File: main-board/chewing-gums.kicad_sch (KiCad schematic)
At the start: 14 parts

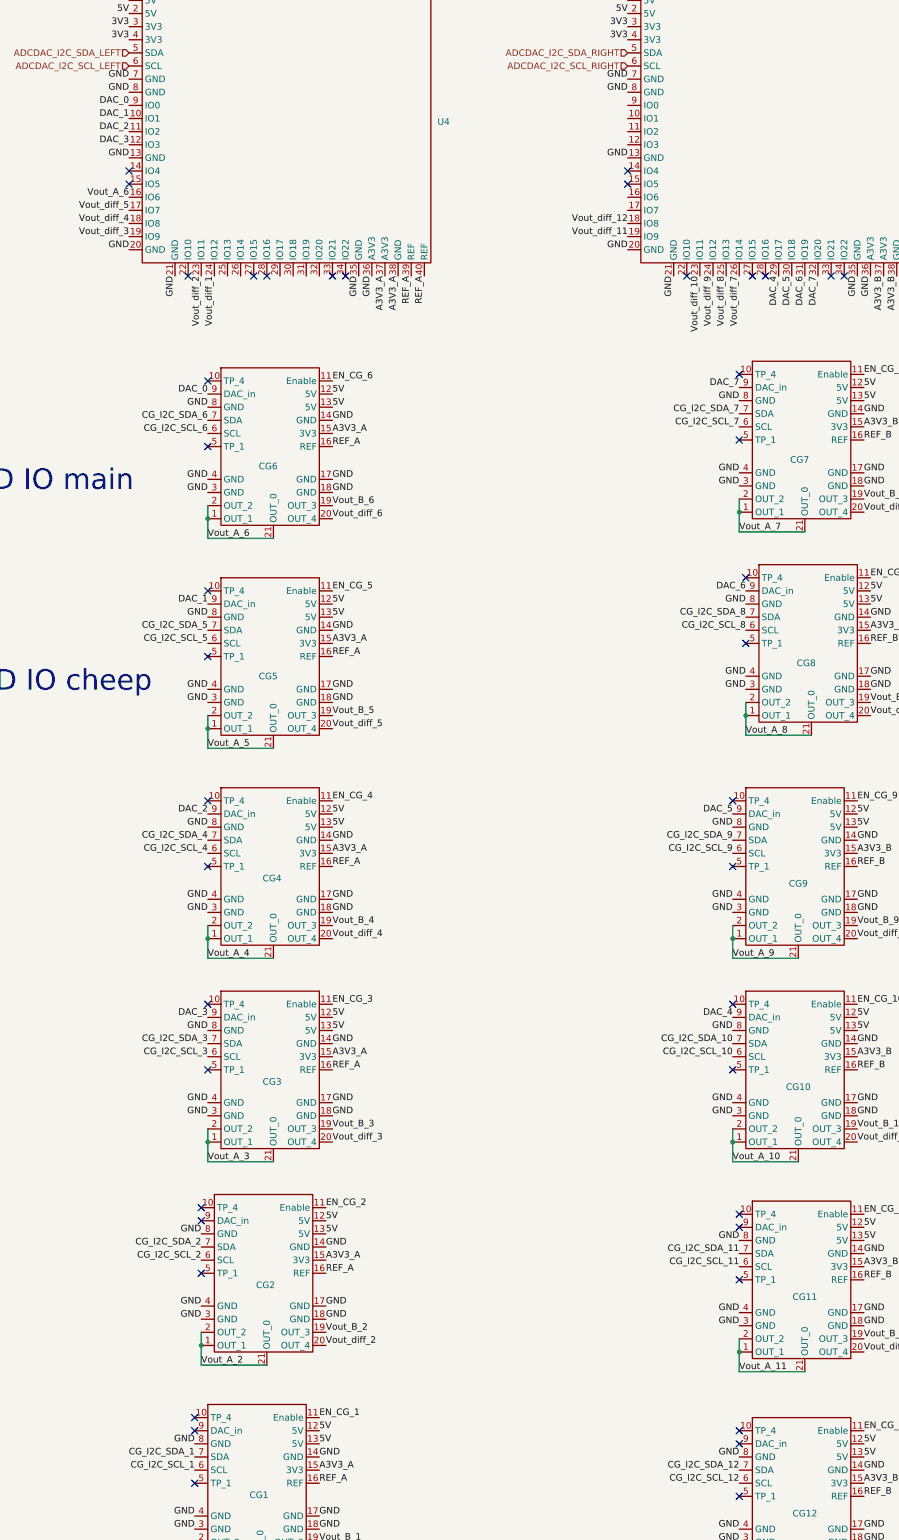
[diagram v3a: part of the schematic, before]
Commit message: Routed all power signals and re-organized GPIOs
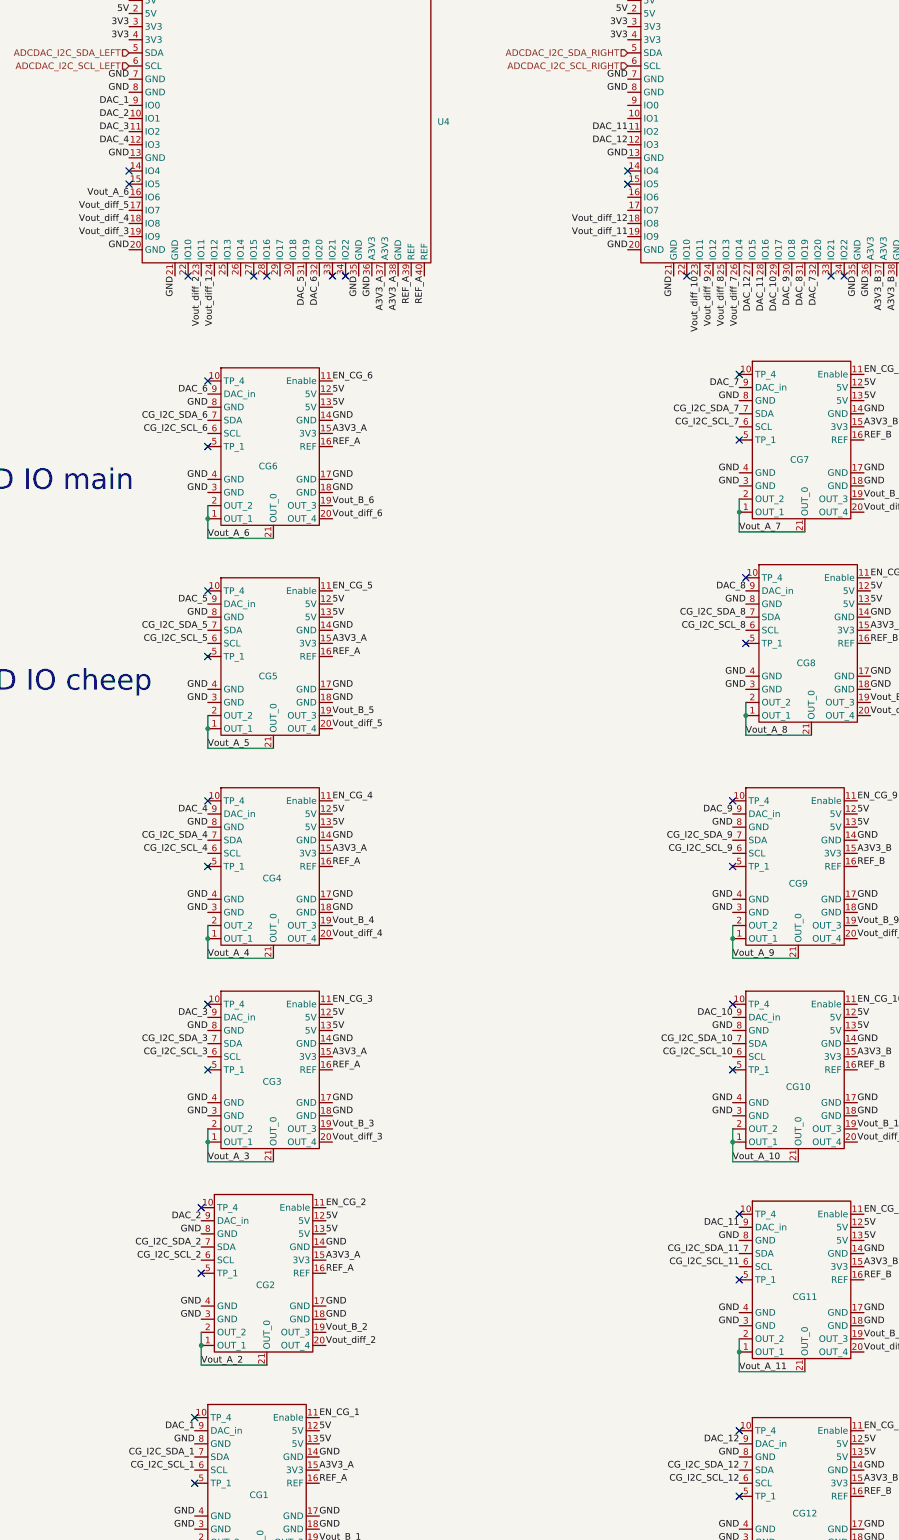
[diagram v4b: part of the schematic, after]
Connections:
- net DAC_1: now also CG1.9 (DAC_in), U4.9 (IO0); no longer CG5.9 (DAC_in), U4.10 (IO1)
- net DAC_2: now also CG2.9 (DAC_in), U4.10 (IO1); no longer CG4.9 (DAC_in), U4.11 (IO2)
- net DAC_3: now also U4.11 (IO2); no longer U4.12 (IO3)
- net DAC_4: now also CG4.9 (DAC_in), U4.12 (IO3); no longer CG10.9 (DAC_in), U5.29 (IO17)
- net DAC_5: now also CG5.9 (DAC_in), U4.31 (IO19); no longer CG9.9 (DAC_in), U5.30 (IO18)
- net DAC_6: now also CG6.9 (DAC_in), U4.32 (IO20); no longer CG8.9 (DAC_in), U5.31 (IO19)
- net DAC_12: now reaches CG12.9 (DAC_in)
- net DAC_12: now also U5.12 (IO3), U5.27 (IO15)
- net DAC_11: now reaches U5.11 (IO2)
- net DAC_11: now also CG11.9 (DAC_in), U5.28 (IO16)
- removed net DAC_0: CG6.9 (DAC_in), U4.9 (IO0)
- new net DAC_10: CG10.9 (DAC_in), U5.29 (IO17)
- new net DAC_8: CG8.9 (DAC_in), U5.31 (IO19)
- new net DAC_9: CG9.9 (DAC_in), U5.30 (IO18)
- no-connect marks 42 -> 36
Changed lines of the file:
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@@
 	)
 	(no_connect
-		(at 86.36 273.05)
-	)
-	(no_connect
 		(at 72.39 72.39)
 	)
@@
 	)
 	(no_connect
-		(at 193.04 90.17)
-	)
-	(no_connect
 		(at 86.36 283.21)
 	)
@@
 	)
 	(no_connect
-		(at 85.09 313.69)
-	)
-	(no_connect
 		(at 87.63 123.19)
 	)
@@
 	)
 	(no_connect
-		(at 195.58 90.17)
-	)
-	(no_connect
 		(at 190.5 326.39)
 	)
@@
 	)
 	(no_connect
-		(at 190.5 316.23)
-	)
-	(no_connect
 		(at 87.63 163.83)
 	)
@@
 	)
 	(no_connect
-		(at 190.5 274.32)
-	)
-	(no_connect
 		(at 168.91 69.85)
 	)
@@
 		)
 	)
-	(label "DAC_4"
+	(label "DAC_10"
 		(at 198.12 90.17 270)
 		(effects
@@
 		)
 	)
-	(label "DAC_6"
+	(label "DAC_8"
 		(at 203.2 90.17 270)
 		(effects
@@
 		)
 	)
+	(label "DAC_1"
+		(at 85.09 313.69 180)
+		(effects
+			(font
+				(size 1.27 1.27)
+			)
+			(justify right bottom)
+		)
+	)
 	(label "5V"
 		(at 111.76 156.21 0)
@@
 		)
 	)
+	(label "DAC_12"
+		(at 193.04 90.17 270)
+		(effects
+			(font
+				(size 1.27 1.27)
+			)
+			(justify right bottom)
+		)
+	)
 	(label "GND"
 		(at 87.63 196.85 180)
@@
 		)
 	)
-	(label "DAC_0"
+	(label "DAC_1"
 		(at 72.39 57.15 180)
 		(effects
@@
 		)
 	)
-	(label "DAC_0"
+	(label "DAC_6"
 		(at 87.63 113.03 180)
 		(effects
@@
 		)
 	)
+	(label "DAC_12"
+		(at 190.5 316.23 180)
+		(effects
+			(font
+				(size 1.27 1.27)
+			)
+			(justify right bottom)
+		)
+	)
 	(label "A3V3_A"
 		(at 124.46 90.17 270)
@@
 		)
 	)
+	(label "DAC_2"
+		(at 86.36 273.05 180)
+		(effects
+			(font
+				(size 1.27 1.27)
+			)
+			(justify right bottom)
+		)
+	)
 	(label "Vout_diff_9"
 		(at 146.05 378.46 180)
@@
 		)
 	)
-	(label "DAC_3"
+	(label "DAC_4"
 		(at 72.39 64.77 180)
 		(effects
@@
 		)
 	)
+	(label "DAC_6"
+		(at 109.22 90.17 270)
+		(effects
+			(font
+				(size 1.27 1.27)
+			)
+			(justify right bottom)
+		)
+	)
 	(label "REF_B"
 		(at 214.63 326.39 0)
@@
 		)
 	)
+	(label "DAC_11"
+		(at 168.91 62.23 180)
+		(effects
+			(font
+				(size 1.27 1.27)
+			)
+			(justify right bottom)
+		)
+	)
 	(label "A3V3_A"
 		(at 111.76 161.29 0)
@@
 		)
 	)
-	(label "DAC_2"
+	(label "DAC_4"
 		(at 87.63 194.31 180)
 		(effects
@@
 		)
 	)
-	(label "DAC_4"
+	(label "DAC_10"
 		(at 189.23 233.68 180)
 		(effects
@@
 		)
 	)
-	(label "DAC_1"
+	(label "DAC_5"
 		(at 87.63 153.67 180)
 		(effects
@@
 		)
 	)
-	(label "DAC_1"
+	(label "DAC_2"
 		(at 72.39 59.69 180)
 		(effects
@@
 		)
 	)
-	(label "DAC_6"
+	(label "DAC_8"
 		(at 191.77 151.13 180)
 		(effects
@@
 		)
 	)
-	(label "DAC_5"
+	(label "DAC_9"
 		(at 189.23 194.31 180)
 		(effects
@@
 		)
 	)
-	(label "DAC_5"
+	(label "DAC_9"
 		(at 200.66 90.17 270)
 		(effects
@@
 		)
 	)
-	(label "DAC_2"
+	(label "DAC_3"
 		(at 72.39 62.23 180)
 		(effects
@@
 		)
 	)
+	(label "DAC_12"
+		(at 168.91 64.77 180)
+		(effects
+			(font
+				(size 1.27 1.27)
+			)
+			(justify right bottom)
+		)
+	)
 	(label "Vout_B_10"
 		(at 213.36 255.27 0)
@@
 		)
 	)
+	(label "DAC_11"
+		(at 195.58 90.17 270)
+		(effects
+			(font
+				(size 1.27 1.27)
+			)
+			(justify right bottom)
+		)
+	)
+	(label "DAC_5"
+		(at 106.68 90.17 270)
+		(effects
+			(font
+				(size 1.27 1.27)
+			)
+			(justify right bottom)
+		)
+	)
 	(label "REF_A"
 		(at 129.54 90.17 270)
@@
 		)
 	)
+	(label "DAC_11"
+		(at 190.5 274.32 180)
+		(effects
+			(font
+				(size 1.27 1.27)
+			)
+			(justify right bottom)
+		)
+	)

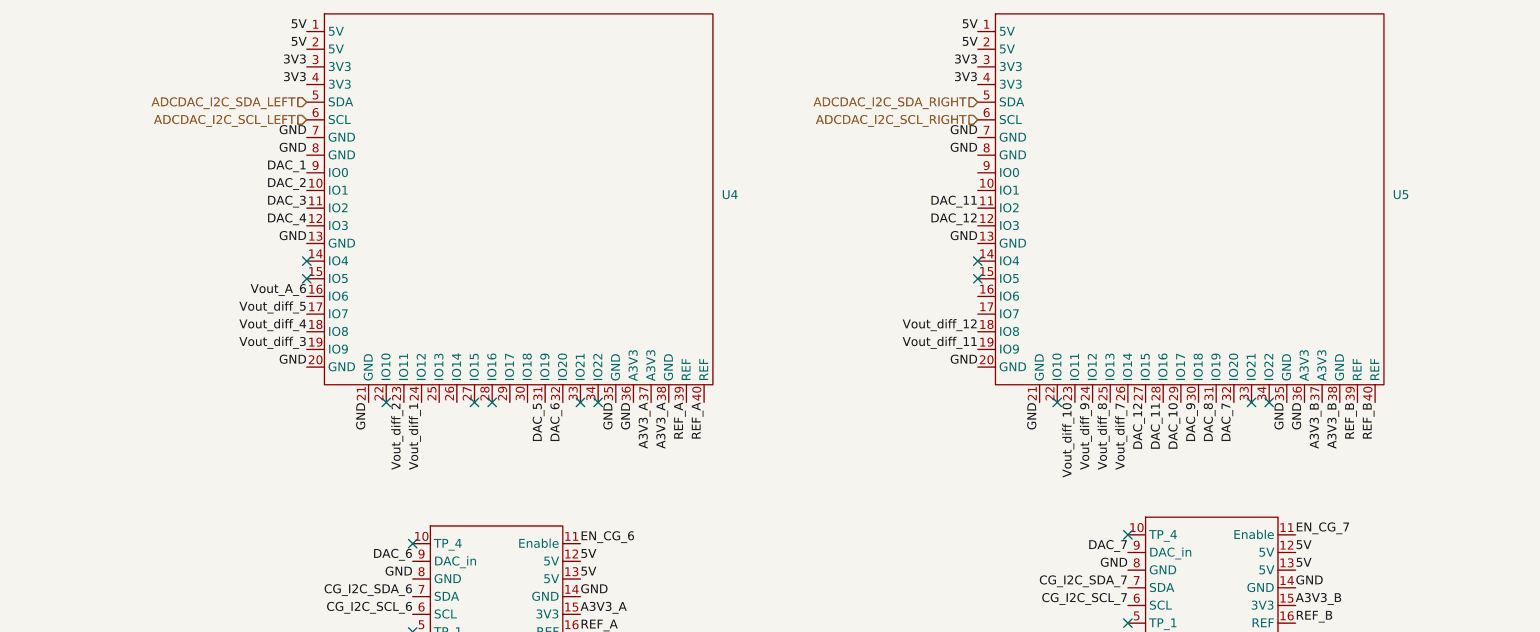
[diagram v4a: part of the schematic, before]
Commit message: rework main PCB: added USB-C, new connector symbol & footprints
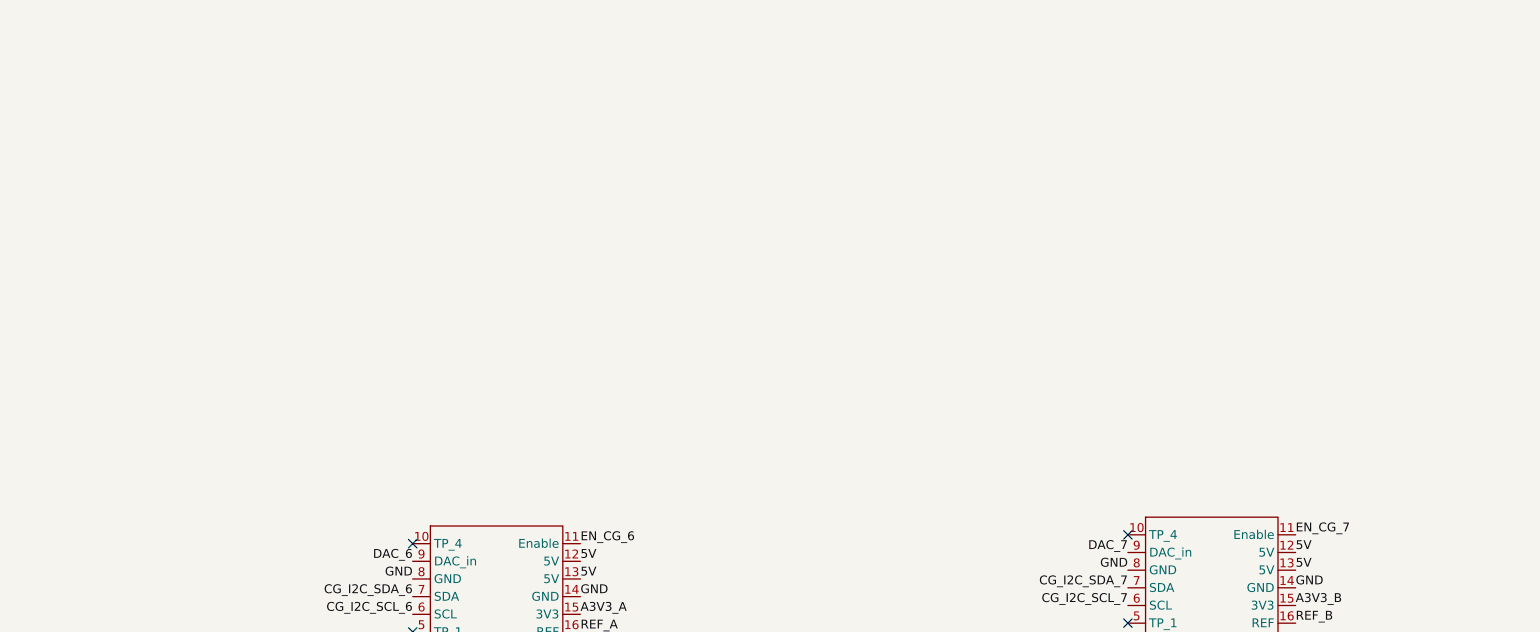
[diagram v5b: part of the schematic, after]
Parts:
- removed U4, U5: ~, heep_footprints:adc-dac, symbol cheeps-tb:adc-dac
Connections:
- no-connect marks 36 -> 24

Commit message: update testing board
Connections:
- net 3V3: now also CG1.A2 (3V3), CG10.A2 (3V3), CG11.A2 (3V3), CG12.A2 (3V3), CG2.A2 (3V3), CG3.A2 (3V3), CG4.A2 (3V3), CG5.A2 (3V3), CG6.A2 (3V3), CG7.A2 (3V3), CG8.A2 (3V3), CG9.A2 (3V3)
- net 5V: now also CG1.A1 (5V), CG1.B1 (5V), CG10.A1 (5V), CG10.B1 (5V), CG11.A1 (5V), CG11.B1 (5V), CG12.A1 (5V), CG12.B1 (5V), CG2.A1 (5V), CG2.B1 (5V), CG3.A1 (5V), CG3.B1 (5V), CG4.A1 (5V), CG4.B1 (5V), CG5.A1 (5V), CG5.B1 (5V), CG6.A1 (5V), CG6.B1 (5V), CG7.A1 (5V), CG7.B1 (5V), CG8.A1 (5V), CG8.B1 (5V), CG9.A1 (5V), CG9.B1 (5V); no longer CG1.12 (5V), CG1.13 (5V), CG10.12 (5V), CG10.13 (5V), CG11.12 (5V), CG11.13 (5V), CG12.12 (5V), CG12.13 (5V), CG2.12 (5V), CG2.13 (5V), CG3.12 (5V), CG3.13 (5V), CG4.12 (5V), CG4.13 (5V), CG5.12 (5V), CG5.13 (5V), CG6.12 (5V), CG6.13 (5V), CG7.12 (5V), CG7.13 (5V), CG8.12 (5V), CG8.13 (5V), CG9.12 (5V), CG9.13 (5V)
- net CG_I2C_SCL_1: now also CG1.A4 (SCL); no longer CG1.6 (SCL)
- net CG_I2C_SCL_10: now also CG10.A4 (SCL); no longer CG10.6 (SCL)
- net CG_I2C_SCL_11: now also CG11.A4 (SCL); no longer CG11.6 (SCL)
- net CG_I2C_SCL_12: now also CG12.A4 (SCL); no longer CG12.6 (SCL)
- net CG_I2C_SCL_2: now also CG2.A4 (SCL); no longer CG2.6 (SCL)
- net CG_I2C_SCL_3: now also CG3.A4 (SCL); no longer CG3.6 (SCL)
- net CG_I2C_SCL_4: now also CG4.A4 (SCL); no longer CG4.6 (SCL)
- net CG_I2C_SCL_5: now also CG5.A4 (SCL); no longer CG5.6 (SCL)
- net CG_I2C_SCL_6: now also CG6.A4 (SCL); no longer CG6.6 (SCL)
- net CG_I2C_SCL_7: now also CG7.A4 (SCL); no longer CG7.6 (SCL)
- net CG_I2C_SCL_8: now also CG8.A4 (SCL); no longer CG8.6 (SCL)
- net CG_I2C_SCL_9: now also CG9.A4 (SCL); no longer CG9.6 (SCL)
- net CG_I2C_SDA_1: now also CG1.A3 (SDA); no longer CG1.7 (SDA)
- net CG_I2C_SDA_10: now also CG10.A3 (SDA); no longer CG10.7 (SDA)
- net CG_I2C_SDA_11: now also CG11.A3 (SDA); no longer CG11.7 (SDA)
- net CG_I2C_SDA_12: now also CG12.A3 (SDA); no longer CG12.7 (SDA)
- net CG_I2C_SDA_2: now also CG2.A3 (SDA); no longer CG2.7 (SDA)
- net CG_I2C_SDA_3: now also CG3.A3 (SDA); no longer CG3.7 (SDA)
- net CG_I2C_SDA_4: now also CG4.A3 (SDA); no longer CG4.7 (SDA)
- net CG_I2C_SDA_5: now also CG5.A3 (SDA); no longer CG5.7 (SDA)
- net CG_I2C_SDA_6: now also CG6.A3 (SDA); no longer CG6.7 (SDA)
- net CG_I2C_SDA_7: now also CG7.A3 (SDA); no longer CG7.7 (SDA)
- net CG_I2C_SDA_8: now also CG8.A3 (SDA); no longer CG8.7 (SDA)
- net CG_I2C_SDA_9: now also CG9.A3 (SDA); no longer CG9.7 (SDA)
- net EN_CG_1: now also CG1.B4 (ENABLE); no longer CG1.11 (Enable)
- net EN_CG_10: now also CG10.B4 (ENABLE); no longer CG10.11 (Enable)
- net EN_CG_11: now also CG11.B4 (ENABLE); no longer CG11.11 (Enable)
- net EN_CG_12: now also CG12.B4 (ENABLE); no longer CG12.11 (Enable)
- net EN_CG_2: now also CG2.B4 (ENABLE); no longer CG2.11 (Enable)
- net EN_CG_3: now also CG3.B4 (ENABLE); no longer CG3.11 (Enable)
- net EN_CG_4: now also CG4.B4 (ENABLE); no longer CG4.11 (Enable)
- net EN_CG_5: now also CG5.B4 (ENABLE); no longer CG5.11 (Enable)
- net EN_CG_6: now also CG6.B4 (ENABLE); no longer CG6.11 (Enable)
- net EN_CG_7: now also CG7.B4 (ENABLE); no longer CG7.11 (Enable)
- net EN_CG_8: now also CG8.B4 (ENABLE); no longer CG8.11 (Enable)
- net EN_CG_9: now also CG9.B4 (ENABLE); no longer CG9.11 (Enable)
- net GND: now also CG1.A5 (GND), CG1.B5 (GND), CG1.C1 (GND), CG1.C6 (GND), CG10.A5 (GND), CG10.B5 (GND), CG10.C1 (GND), CG10.C6 (GND), CG11.A5 (GND), CG11.B5 (GND), CG11.C1 (GND), CG11.C6 (GND), CG12.A5 (GND), CG12.B5 (GND), CG12.C1 (GND), CG12.C6 (GND), CG2.A5 (GND), CG2.B5 (GND), CG2.C1 (GND), CG2.C6 (GND), CG3.A5 (GND), CG3.B5 (GND), CG3.C1 (GND), CG3.C6 (GND), CG4.A5 (GND), CG4.B5 (GND), CG4.C1 (GND), CG4.C6 (GND), CG5.A5 (GND), CG5.B5 (GND), CG5.C1 (GND), CG5.C6 (GND), CG6.A5 (GND), CG6.B5 (GND), CG6.C1 (GND), CG6.C6 (GND), CG7.A5 (GND), CG7.B5 (GND), CG7.C1 (GND), CG7.C6 (GND), CG8.A5 (GND), CG8.B5 (GND), CG8.C1 (GND), CG8.C6 (GND), CG9.A5 (GND), CG9.B5 (GND), CG9.C1 (GND), CG9.C6 (GND); no longer CG1.14 (GND), CG1.17 (GND), CG1.18 (GND), CG1.3 (GND), CG1.4 (GND), CG1.8 (GND), CG10.14 (GND), CG10.17 (GND), CG10.18 (GND), CG10.3 (GND), CG10.4 (GND), CG10.8 (GND), CG11.14 (GND), CG11.17 (GND), CG11.18 (GND), CG11.3 (GND), CG11.4 (GND), CG11.8 (GND), CG12.14 (GND), CG12.17 (GND), CG12.18 (GND), CG12.3 (GND), CG12.4 (GND), CG12.8 (GND), CG2.14 (GND), CG2.17 (GND), CG2.18 (GND), CG2.3 (GND), CG2.4 (GND), CG2.8 (GND), CG3.14 (GND), CG3.17 (GND), CG3.18 (GND), CG3.3 (GND), CG3.4 (GND), CG3.8 (GND), CG4.14 (GND), CG4.17 (GND), CG4.18 (GND), CG4.3 (GND), CG4.4 (GND), CG4.8 (GND), CG5.14 (GND), CG5.17 (GND), CG5.18 (GND), CG5.3 (GND), CG5.4 (GND), CG5.8 (GND), CG6.14 (GND), CG6.17 (GND), CG6.18 (GND), CG6.3 (GND), CG6.4 (GND), CG6.8 (GND), CG7.14 (GND), CG7.17 (GND), CG7.18 (GND), CG7.3 (GND), CG7.4 (GND), CG7.8 (GND), CG8.14 (GND), CG8.17 (GND), CG8.18 (GND), CG8.3 (GND), CG8.4 (GND), CG8.8 (GND), CG9.14 (GND), CG9.17 (GND), CG9.18 (GND), CG9.3 (GND), CG9.4 (GND), CG9.8 (GND)
- net Vout_A_1: now also CG1.C2 (OUT_1), CG1.C3 (OUT_2), CG1.D1 (OUT_0); no longer CG1.1 (OUT_1), CG1.2 (OUT_2), CG1.21 (OUT_0)
- net Vout_A_10: now also CG10.C2 (OUT_1), CG10.C3 (OUT_2), CG10.D1 (OUT_0); no longer CG10.1 (OUT_1), CG10.2 (OUT_2), CG10.21 (OUT_0)
- net Vout_A_11: now also CG11.C2 (OUT_1), CG11.C3 (OUT_2), CG11.D1 (OUT_0); no longer CG11.1 (OUT_1), CG11.2 (OUT_2), CG11.21 (OUT_0)
- net Vout_A_12: now also CG12.C2 (OUT_1), CG12.C3 (OUT_2), CG12.D1 (OUT_0); no longer CG12.1 (OUT_1), CG12.2 (OUT_2), CG12.21 (OUT_0)
- net Vout_A_2: now also CG2.C2 (OUT_1), CG2.C3 (OUT_2), CG2.D1 (OUT_0); no longer CG2.1 (OUT_1), CG2.2 (OUT_2), CG2.21 (OUT_0)
- net Vout_A_3: now also CG3.C2 (OUT_1), CG3.C3 (OUT_2), CG3.D1 (OUT_0); no longer CG3.1 (OUT_1), CG3.2 (OUT_2), CG3.21 (OUT_0)
- net Vout_A_4: now also CG4.C2 (OUT_1), CG4.C3 (OUT_2), CG4.D1 (OUT_0); no longer CG4.1 (OUT_1), CG4.2 (OUT_2), CG4.21 (OUT_0)
- net Vout_A_5: now also CG5.C2 (OUT_1), CG5.C3 (OUT_2), CG5.D1 (OUT_0); no longer CG5.1 (OUT_1), CG5.2 (OUT_2), CG5.21 (OUT_0)
- net Vout_A_6: now also CG6.C2 (OUT_1), CG6.C3 (OUT_2), CG6.D1 (OUT_0); no longer CG6.1 (OUT_1), CG6.2 (OUT_2), CG6.21 (OUT_0)
- net Vout_A_7: now also CG7.C2 (OUT_1), CG7.C3 (OUT_2), CG7.D1 (OUT_0); no longer CG7.1 (OUT_1), CG7.2 (OUT_2), CG7.21 (OUT_0)
- net Vout_A_8: now also CG8.C2 (OUT_1), CG8.C3 (OUT_2), CG8.D1 (OUT_0); no longer CG8.1 (OUT_1), CG8.2 (OUT_2), CG8.21 (OUT_0)
- net Vout_A_9: now also CG9.C2 (OUT_1), CG9.C3 (OUT_2), CG9.D1 (OUT_0); no longer CG9.1 (OUT_1), CG9.2 (OUT_2), CG9.21 (OUT_0)
- net Vout_B_1: now also CG1.C5 (OUT_4); no longer CG1.19 (OUT_3)
- net Vout_B_10: now also CG10.C5 (OUT_4); no longer CG10.19 (OUT_3)
- net Vout_B_11: now also CG11.C5 (OUT_4); no longer CG11.19 (OUT_3)
- net Vout_B_12: now also CG12.C5 (OUT_4); no longer CG12.19 (OUT_3)
- net Vout_B_2: now also CG2.C5 (OUT_4); no longer CG2.19 (OUT_3)
- net Vout_B_3: now also CG3.C5 (OUT_4); no longer CG3.19 (OUT_3)
- net Vout_B_4: now also CG4.C5 (OUT_4); no longer CG4.19 (OUT_3)
- net Vout_B_5: now also CG5.C5 (OUT_4); no longer CG5.19 (OUT_3)
- net Vout_B_6: now also CG6.C5 (OUT_4); no longer CG6.19 (OUT_3)
- net Vout_B_7: now also CG7.C5 (OUT_4); no longer CG7.19 (OUT_3)
- net Vout_B_8: now also CG8.C5 (OUT_4); no longer CG8.19 (OUT_3)
- net Vout_B_9: now also CG9.C5 (OUT_4); no longer CG9.19 (OUT_3)
- net Vout_diff_1: now also CG1.C4 (OUT_3); no longer CG1.20 (OUT_4)
- net Vout_diff_10: now also CG10.C4 (OUT_3); no longer CG10.20 (OUT_4)
- net Vout_diff_11: now also CG11.C4 (OUT_3); no longer CG11.20 (OUT_4)
- net Vout_diff_12: now also CG12.C4 (OUT_3); no longer CG12.20 (OUT_4)
- net Vout_diff_2: now also CG2.C4 (OUT_3); no longer CG2.20 (OUT_4)
- net Vout_diff_3: now also CG3.C4 (OUT_3); no longer CG3.20 (OUT_4)
- net Vout_diff_4: now also CG4.C4 (OUT_3); no longer CG4.20 (OUT_4)
- net Vout_diff_5: now also CG5.C4 (OUT_3); no longer CG5.20 (OUT_4)
- net Vout_diff_6: now also CG6.C4 (OUT_3); no longer CG6.20 (OUT_4)
- net Vout_diff_7: now also CG7.C4 (OUT_3); no longer CG7.20 (OUT_4)
- net Vout_diff_8: now also CG8.C4 (OUT_3); no longer CG8.20 (OUT_4)
- net Vout_diff_9: now also CG9.C4 (OUT_3); no longer CG9.20 (OUT_4)
- removed net A3V3_A: CG1.15 (3V3), CG2.15 (3V3), CG3.15 (3V3), CG4.15 (3V3), CG5.15 (3V3), CG6.15 (3V3)
- removed net A3V3_B: CG10.15 (3V3), CG11.15 (3V3), CG12.15 (3V3), CG7.15 (3V3), CG8.15 (3V3), CG9.15 (3V3)
- removed net DAC_1: CG1.9 (DAC_in)
- removed net DAC_10: CG10.9 (DAC_in)
- removed net DAC_11: CG11.9 (DAC_in)
- removed net DAC_12: CG12.9 (DAC_in)
- removed net DAC_2: CG2.9 (DAC_in)
- removed net DAC_3: CG3.9 (DAC_in)
- removed net DAC_4: CG4.9 (DAC_in)
- removed net DAC_5: CG5.9 (DAC_in)
- removed net DAC_6: CG6.9 (DAC_in)
- removed net DAC_7: CG7.9 (DAC_in)
- removed net DAC_8: CG8.9 (DAC_in)
- removed net DAC_9: CG9.9 (DAC_in)
- removed net REF_A: CG1.16 (REF), CG2.16 (REF), CG3.16 (REF), CG4.16 (REF), CG5.16 (REF), CG6.16 (REF)
- removed net REF_B: CG10.16 (REF), CG11.16 (REF), CG12.16 (REF), CG7.16 (REF), CG8.16 (REF), CG9.16 (REF)
- new net -5V: CG1.B3 (-5V), CG10.B3 (-5V), CG11.B3 (-5V), CG12.B3 (-5V), CG2.B3 (-5V), CG3.B3 (-5V), CG4.B3 (-5V), CG5.B3 (-5V), CG6.B3 (-5V), CG7.B3 (-5V), CG8.B3 (-5V), CG9.B3 (-5V)
- new net VDDIO: CG1.B2 (3V3), CG10.B2 (3V3), CG11.B2 (3V3), CG12.B2 (3V3), CG2.B2 (3V3), CG3.B2 (3V3), CG4.B2 (3V3), CG5.B2 (3V3), CG6.B2 (3V3), CG7.B2 (3V3), CG8.B2 (3V3), CG9.B2 (3V3)
- no-connect marks 24 -> 0
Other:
- note removed: "VDD IO cheep"
- note removed: "VDD IO main"
